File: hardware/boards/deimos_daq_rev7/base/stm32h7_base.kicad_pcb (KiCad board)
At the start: 4 copper layers, 196 parts, among them IC1 STM32H743ZIT6, IC10001 TPS560430XDBVR, IC10002 TPS560430XDBVR, IC4001 TPS560430XDBVR, IC5004 REF35102QDBVR, IC8001 INA826AIDR, J3001 RCH_RC01133, J4 Conn_02x07_Odd_Even, J8001 Barrel_Jack PJ-202BH, T1 H1102NLT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

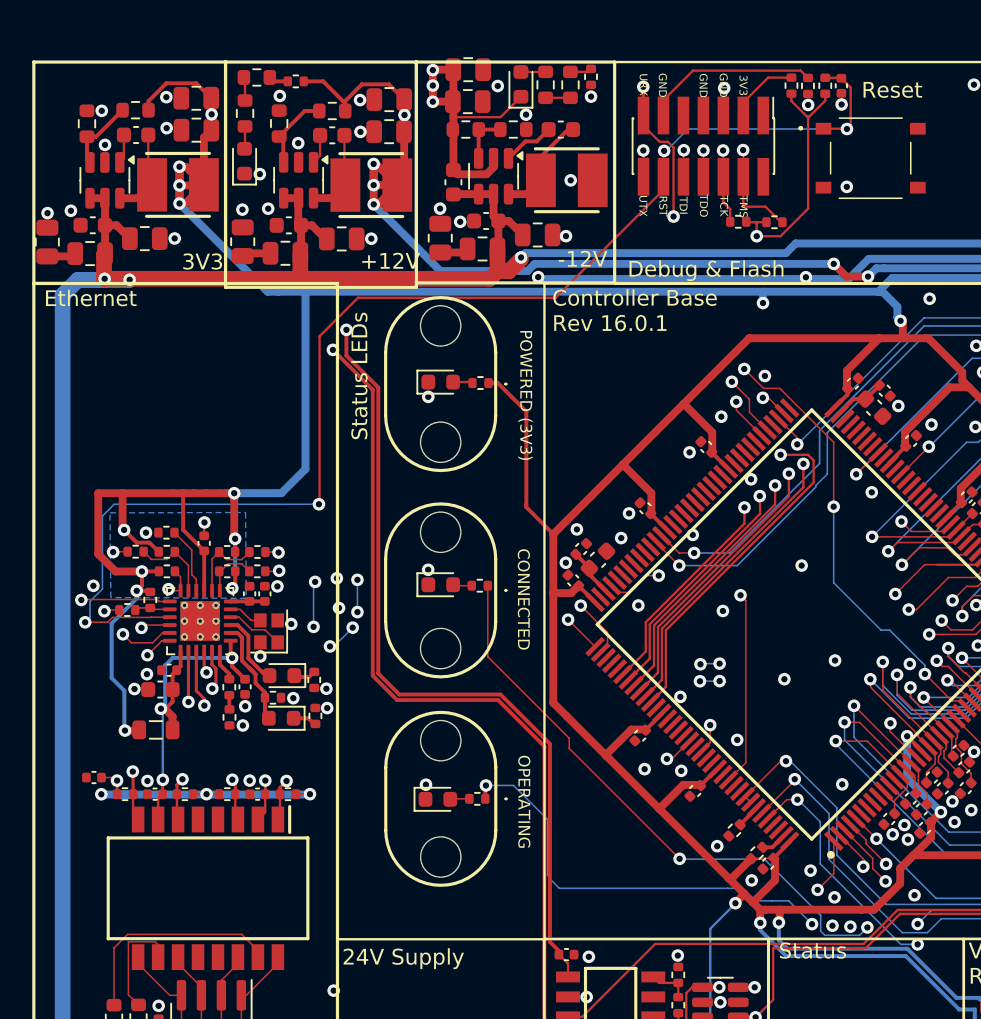
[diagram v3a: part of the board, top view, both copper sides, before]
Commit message: resolve drc lints
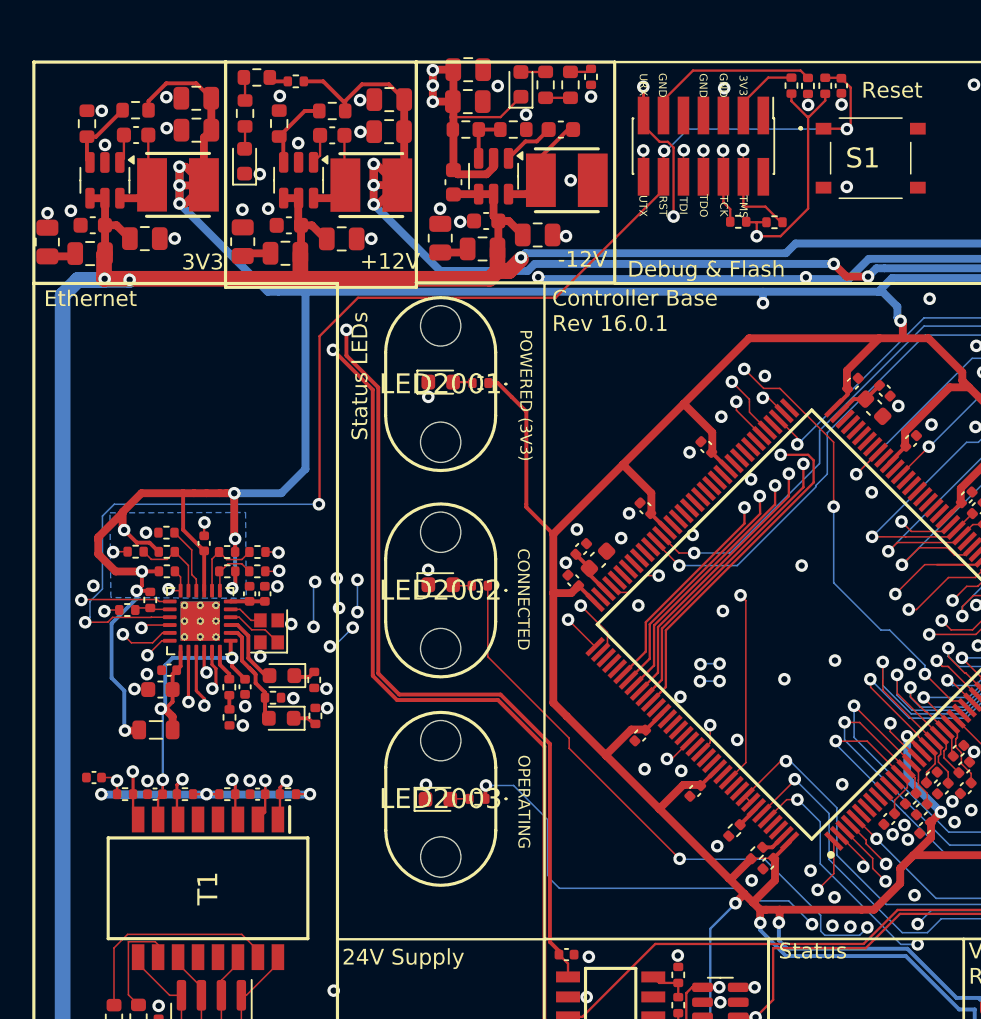
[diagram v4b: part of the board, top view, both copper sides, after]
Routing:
- net +3V3: track 503.6 -> 502.8 mm, vias 24 -> 23
- net /Micro/RMII_TXD1: track 64.4 -> 65.0 mm
- net /Micro/RMII_RXD1: track 54.4 -> 54.9 mm
- net +12V: vias 10 -> 9
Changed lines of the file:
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@@
 			(at -0.5 0 0)
 			(layer "F.SilkS")
-			(hide yes)
 			(effects
 				(font
@@
 			(at 0 0 180)
 			(layer "F.SilkS")
-			(hide yes)
 			(effects
 				(font
@@
 			(at 0 0 -90)
 			(layer "F.SilkS")
-			(hide yes)
 			(effects
 				(font
@@
 			(at 0 0 180)
 			(layer "F.SilkS")
-			(hide yes)
 			(effects
 				(font
@@
 			(at 0 0 180)
 			(layer "F.SilkS")
-			(hide yes)
 			(effects
 				(font
@@
 	)
 	(segment
-		(start 46.492 97.9685)
-		(end 46.492 100.2095)
-		(width 0.5)
+		(start 104.899924 103.970702)
+		(end 106.377949 102.492677)
+		(width 0.1)
 		(layer "F.Cu")
 		(net 2)
 	)
 	(segment
-		(start 104.899924 103.970702)
-		(end 106.377949 102.492677)
-		(width 0.1)
+		(start 46.492 99.22)
+		(end 46.492 100.2095)
+		(width 0.5)
 		(layer "F.Cu")
 		(net 2)
@@
 	)
 	(segment
+		(start 44.942 100.77)
+		(end 46.492 99.22)
+		(width 0.5)
+		(layer "F.Cu")
+		(net 2)
+	)
+	(segment
 		(start 101.62 130.805)
 		(end 101.485 130.67)
@@
 	)
 	(segment
+		(start 52.1348 74.872896)
+		(end 52.1348 72.850396)
+		(width 0.5)
+		(layer "F.Cu")
+		(net 2)
+	)
+	(segment
 		(start 46.59 100.3075)
 		(end 46.58 100.2975)
@@
 	)
 	(segment
+		(start 46.492 99.22)
+		(end 46.492 99.1665)
+		(width 0.5)
+		(layer "F.Cu")
+		(net 2)
+	)
+	(segment
 		(start 77.264127 114.587278)
 		(end 78.85096 113.000445)
@@
 	)
 	(segment
-		(start 44.942 97.9685)
-		(end 44.942 101.838303)
-		(width 0.5)
-		(layer "F.Cu")
-		(net 2)
-	)
-	(segment
 		(start 88.342774 81.62)
 		(end 90.1 79.862774)
@@
 	)
 	(segment
+		(start 46.492 99.1665)
+		(end 47.69 97.9685)
+		(width 0.5)
+		(layer "F.Cu")
+		(net 2)
+	)
+	(segment
 		(start 88.29 124.461499)
 		(end 87.419127 124.461499)
@@
 	)
 	(segment
-		(start 49.722 97.9685)
-		(end 50.342 97.9685)
-		(width 0.5)
-		(layer "F.Cu")
-		(net 2)
-	)
-	(segment
 		(start 94.289788 124.461499)
 		(end 93.504127 124.461499)
@@
 	)
 	(segment
-		(start 46.492 97.9685)
-		(end 49.722 97.9685)
-		(width 0.5)
-		(layer "F.Cu")
-		(net 2)
-	)
-	(segment
 		(start 100.339127 91.231499)
 		(end 103.649127 94.541499)
@@
 	)
 	(segment
+		(start 44.942 100.93)
+		(end 44.942 101.838303)
+		(width 0.5)
+		(layer "F.Cu")
+		(net 2)
+	)
+	(segment
 		(start 103.649127 94.541499)
 		(end 107.429127 98.321499)
@@
 	)
 	(segment
-		(start 44.942 97.9685)
-		(end 46.492 97.9685)
-		(width 0.5)
-		(layer "F.Cu")
-		(net 2)
-	)
-	(segment
 		(start 90.1 79.862774)
 		(end 90.1 74.03)
@@
 	)
 	(segment
+		(start 47.69 97.9685)
+		(end 50.342 97.9685)
+		(width 0.5)
+		(layer "F.Cu")
+		(net 2)
+	)
+	(segment
+		(start 52.1348 72.850396)
+		(end 52.1273 72.842896)
+		(width 0.5)
+		(layer "F.Cu")
+		(net 2)
+	)
+	(segment
 		(start 90.153173 74.03)
 		(end 90.1 74.03)
@@
 	)
 	(segment
+		(start 44.942 100.93)
+		(end 44.942 100.77)
+		(width 0.5)
+		(layer "F.Cu")
+		(net 2)
+	)
+	(segment
 		(start 101.025 136.27)
 		(end 101.025 135.465)
@@
 	)
 	(via
-		(at 52.1548 73.865396)
-		(size 0.8)
-		(drill 0.4)
-		(layers "F.Cu" "B.Cu")
-		(net 2)
-	)
-	(via
 		(at 87.06 125.3)
 		(size 0.8)
@@
 	)
 	(segment
-		(start 101.280797 102.087344)
-		(end 100.856794 102.511347)
-		(width 0.1)
-		(layer "F.Cu")
-		(net 39)
-	)
-	(segment
 		(start 97.518653 102.511347)
 		(end 95.65 104.38)
@@
 	)
 	(segment
+		(start 101.280797 102.087344)
+		(end 100.856794 102.511347)
+		(width 0.1)
+		(layer "F.Cu")
+		(net 39)
+	)
+	(segment
 		(start 100.856794 102.511347)
 		(end 97.518653 102.511347)
@@
 	)
 	(segment
+		(start 62.17 104.69)
+		(end 61.81 104.69)
+		(width 0.1)
+		(layer "In2.Cu")
+		(net 39)
+	)
+	(segment
 		(start 75.462842 107.4)
 		(end 73.36 107.4)
@@
 	)
 	(segment
-		(start 62.17 104.69)
-		(end 62.119999 104.69)
+		(start 59.6435 102.9035)
+		(end 56.452 102.9035)
 		(width 0.1)
 		(layer "In2.Cu")
@@
 	)
 	(segment
-		(start 59.6435 102.9035)
-		(end 56.452 102.9035)
+		(start 61.81 104.69)
+		(end 60.84 104.69)
 		(width 0.1)
 		(layer "In2.Cu")
@@
 	)
 	(segment
-		(start 70.65 104.69)
-		(end 62.17 104.69)
+		(start 61.81 104.69)
+		(end 62.4 104.69)
 		(width 0.1)
 		(layer "In2.Cu")
@@
 	)
 	(segment
+		(start 70.65 104.69)
+		(end 62.4 104.69)
+		(width 0.1)
+		(layer "In2.Cu")
+		(net 39)
+	)
+	(segment
 		(start 82.61 106.69)
 		(end 76.172842 106.69)
@@
 	)
 	(segment
-		(start 62.17 104.69)
-		(end 60.84 104.69)
+		(start 62.4 104.69)
+		(end 62.17 104.69)
 		(width 0.1)
 		(layer "In2.Cu")
@@
 	)
 	(segment
+		(start 54.82 105.4459)
+		(end 53.3141 105.4459)
+		(width 0.1)
+		(layer "In2.Cu")
+		(net 80)
+	)
+	(segment
 		(start 86.442656 104.177344)
 		(end 86.442656 104.69797)
@@
 	)
 	(segment
-		(start 55.46 105.4459)
-		(end 55.2341 105.4459)
+		(start 54.82 105.4459)
+		(end 55.68 105.4459)
 		(width 0.1)
 		(layer "In2.Cu")
@@
 	)
 	(segment
-		(start 57.6159 105.4459)
-		(end 55.46 105.4459)
-		(width 0.1)
-		(layer "In2.Cu")
-		(net 80)
-	)
-	(segment
 		(start 53.13 105.63)
 		(end 53.13 107.55)
@@
 	)
 	(segment
+		(start 55.46 105.4459)
+		(end 54.82 105.4459)
+		(width 0.1)
+		(layer "In2.Cu")
+		(net 80)
+	)
+	(segment
 		(start 59.25 104.09)
 		(end 58.77 103.61)
@@
 	)
 	(segment
-		(start 55.46 105.4459)
-		(end 53.3141 105.4459)
+		(start 57.6159 105.4459)
+		(end 55.68 105.4459)
+		(width 0.1)
+		(layer "In2.Cu")
+		(net 80)
+	)
+	(segment
+		(start 55.68 105.4459)
+		(end 55.46 105.4459)
 		(width 0.1)
 		(layer "In2.Cu")
@@
 	)
 	(segment
-		(start 73.675 122.425)
-		(end 73.525 122.275)
-		(width 0.1)
-		(layer "B.Cu")
-		(net 163)
-	)
-	(segment
-		(start 71.36 116.56)
-		(end 69.60625 116.56)
-		(width 0.1)
-		(layer "B.Cu")
-		(net 163)
-	)
-	(segment
-		(start 74.275 123.1)
-		(end 73.675 122.5)
+		(start 73.365 118.565)
+		(end 71.36 116.56)
 		(width 0.1)
 		(layer "B.Cu")
@@
 	)
 	(segment
-		(start 86.675 123.9)
-		(end 86.3 123.525)
+		(start 73.525 118.725)
+		(end 73.525 122.275)
 		(width 0.1)
 		(layer "B.Cu")
@@
 	)
 	(segment
-		(start 73.525 118.725)
-		(end 71.36 116.56)
+		(start 71.36 116.56)
+		(end 69.60625 116.56)
 		(width 0.1)
 		(layer "B.Cu")
@@
 	(segment
 		(start 85.875 123.1)
-		(end 84.975 123.1)
+		(end 86.675 123.9)
 		(width 0.1)
 		(layer "B.Cu")
@@
 	)
 	(segment
-		(start 86.3 123.525)
+		(start 74.275 123.1)
 		(end 85.875 123.1)
 		(width 0.1)
@@
 	)
 	(segment
-		(start 88.867628 123.9)
-		(end 87.825 123.9)
+		(start 73.675 122.425)
+		(end 73.675 122.5)
 		(width 0.1)
 		(layer "B.Cu")
@@
 	)
 	(segment
-		(start 73.675 122.5)
-		(end 73.675 122.425)
+		(start 86.675 123.9)
+		(end 88.867628 123.9)
 		(width 0.1)
 		(layer "B.Cu")
@@
 	)
 	(segment
-		(start 73.525 122.275)
+		(start 73.365 118.565)
 		(end 73.525 118.725)
 		(width 0.1)
@@
 	)
 	(segment
-		(start 73.525 118.725)
-		(end 73.525 118.675)
-		(width 0.1)
-		(layer "B.Cu")
-		(net 163)
-	)
-	(segment
-		(start 90.349127 125.381499)
-		(end 88.867628 123.9)
+		(start 88.867628 123.9)
+		(end 90.349127 125.381499)
 		(width 0.1)
 		(layer "B.Cu")
@@
 	)
 	(segment
-		(start 84.975 123.1)
+		(start 73.675 122.5)
 		(end 74.275 123.1)
 		(width 0.1)
@@
 	)
 	(segment
-		(start 87.825 123.9)
-		(end 86.675 123.9)
+		(start 73.525 122.275)
+		(end 73.675 122.425)
 		(width 0.1)
 		(layer "B.Cu")
@@
 		(size 0.8)
 		(drill 0.4)
-		(layers "F.Cu" "B.Cu")
-		(net 177)
-	)
-	(via
-		(at 64.4232 73.9082)
-		(size 0.8)
-		(drill 0.4)

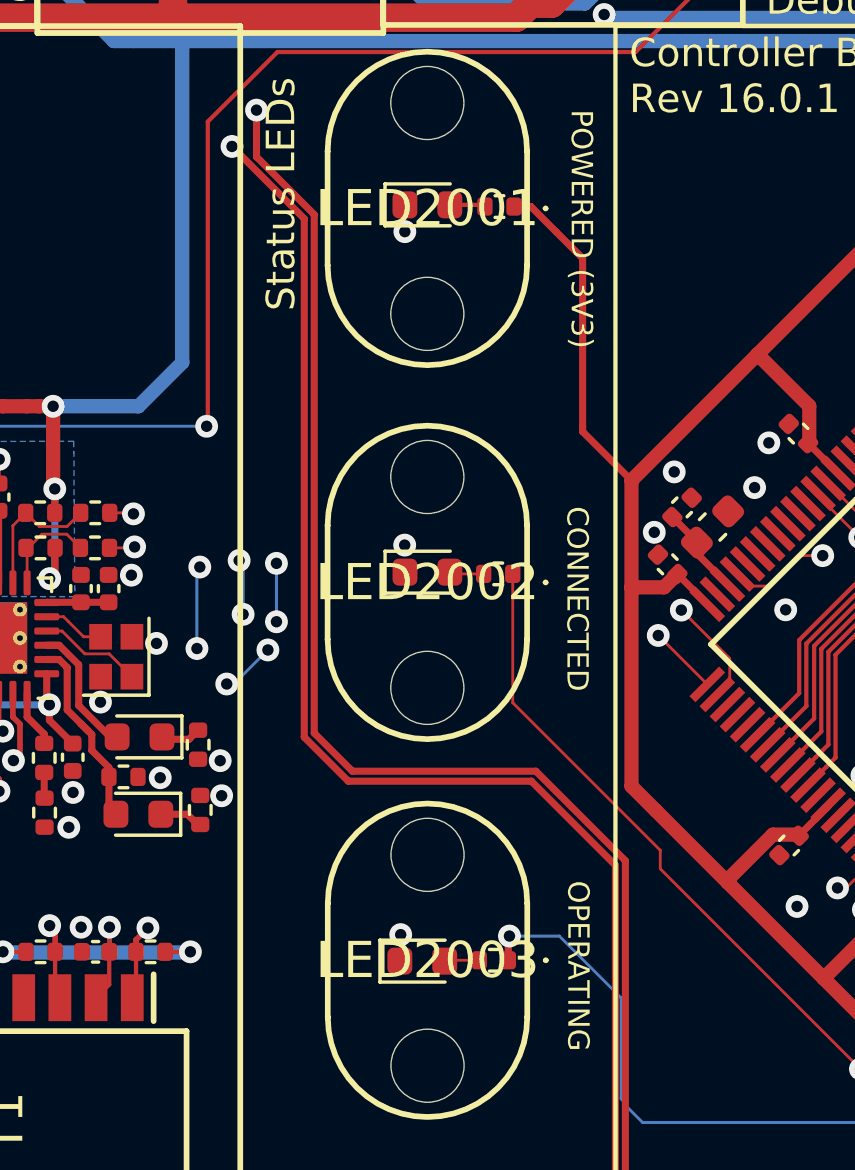
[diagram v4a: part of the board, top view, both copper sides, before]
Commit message: rev 7.0.1 hardware with fixed shunt, increased LED power, and added cutout for light pipes
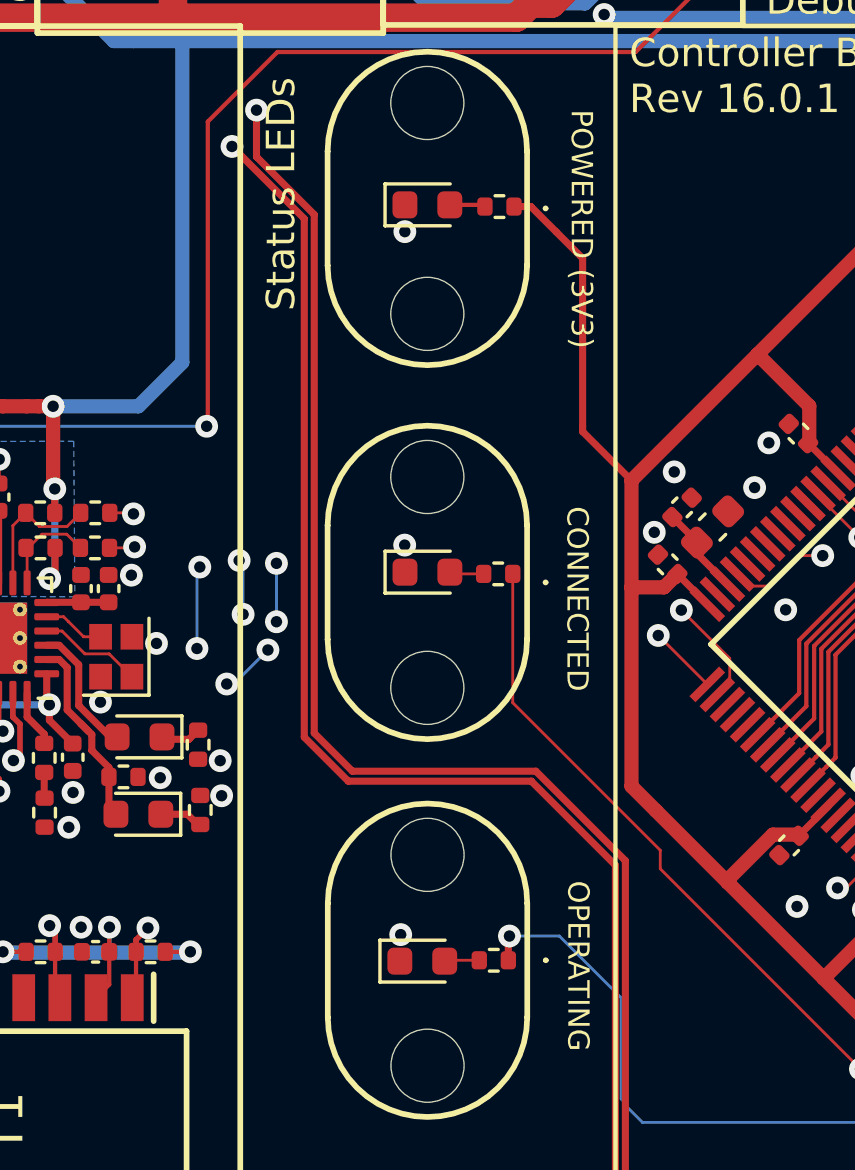
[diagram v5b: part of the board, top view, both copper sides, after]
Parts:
- R2002, R5, R50, R53, R55: value 10k -> 1k
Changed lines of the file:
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@@
 			)
 		)
-		(property "Value" "10k"
+		(property "Value" "1k"
 			(at 0 1.17 0)
 			(layer "F.Fab")
@@
 			)
 		)
-		(property "LCSC" "C25744"
+		(property "LCSC" "C11702"
 			(at 0 0 0)
 			(layer "F.Fab")
@@
 			(at 0 0 180)
 			(layer "F.SilkS")
+			(hide yes)
 			(effects
 				(font
@@
 			)
 		)
-		(property "Value" "10k"
+		(property "Value" "1k"
 			(at 0 1.17 0)
 			(layer "F.Fab")
@@
 			)
 		)
-		(property "LCSC" "C25744"
+		(property "LCSC" "C11702"
 			(at 0 0 0)
 			(layer "F.Fab")
@@
 			)
 		)
-		(property "Value" "10k"
+		(property "Value" "1k"
 			(at 0 1.17 0)
 			(layer "F.Fab")
@@
 			)
 		)
-		(property "LCSC" "C25744"
+		(property "LCSC" "C11702"
 			(at 0 0 0)
 			(layer "F.Fab")
@@
 			)
 		)
-		(property "Value" "10k"
+		(property "Value" "1k"
 			(at 0 1.17 0)
 			(layer "F.Fab")
@@
 			)
 		)
-		(property "LCSC" "C25744"
+		(property "LCSC" "C11702"
 			(at 0 0 0)
 			(layer "F.Fab")
@@
 			(at 0 0 180)
 			(layer "F.SilkS")
+			(hide yes)
 			(effects
 				(font
@@
 			(at 0 0 180)
 			(layer "F.SilkS")
+			(hide yes)
 			(effects
 				(font
@@
 			)
 		)
-		(property "Value" "10k"
+		(property "Value" "1k"
 			(at 0 1.17 0)
 			(layer "F.Fab")
@@
 			)
 		)
-		(property "LCSC" "C25744"
+		(property "LCSC" "C11702"
 			(at 0 0 0)
 			(unlocked yes)
